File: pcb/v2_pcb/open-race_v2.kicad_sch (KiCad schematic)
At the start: 0 parts

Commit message: fnish micro sd card
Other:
- added sheet MicroSD (MicroSD.kicad_sch)
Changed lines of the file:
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@@
+	)
+	(sheet
+		(at 55.88 137.16)
+		(size 43.18 9.525)
+		(exclude_from_sim no)
+		(in_bom yes)
+		(on_board yes)
+		(dnp no)
+		(fields_autoplaced yes)
+		(stroke
+			(width 0.1524)
+			(type solid)
+		)
+		(fill
+			(color 0 0 0 0)
+		)
+		(property "Sheetname" "MicroSD"
+			(at 55.88 136.4484 0)
+			(show_name no)
+			(do_not_autoplace no)
+			(effects
+				(font
+					(size 1.27 1.27)
+				)
+				(justify left bottom)
+			)
+		)
+		(property "Sheetfile" "MicroSD.kicad_sch"
+			(at 55.88 147.2696 0)
+			(show_name no)
+			(do_not_autoplace no)
+			(effects
+				(font
+					(size 1.27 1.27)
+				)
+				(justify left top)
+			)
+		)
+		(instances
+			(project "open-race_v2"
+				(path "/1cc14db4-4207-4c76-b5f6-6a2491c5fa6b"
+					(page "9")
+				)
+			)
+		)
 	)
 	(sheet

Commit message: run load switch
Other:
- sheet Power ports: added PWR_ON; removed none
- sheet STM32_MCU_IO ports: added PWR_ON; removed none
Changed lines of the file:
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@@
 	(generator_version "10.0")
 	(paper "A4")
+	(wire
+		(pts
+			(xy 99.06 127) (xy 116.84 127)
+		)
+		(stroke
+			(width 0)
+			(type default)
+		)
+	)
 	(sheet
 		(at 55.88 83.82)
@@
 			)
 		)
+		(pin "PWR_ON" output
+			(at 116.84 127 180)
+			(effects
+				(font
+					(size 1.27 1.27)
+				)
+				(justify right)
+			)
+		)
 		(instances
 			(project "open-race_v2"
@@
 			)
 		)
+		(pin "PWR_ON" input
+			(at 99.06 127 0)
+			(effects
+				(font
+					(size 1.27 1.27)
+				)
+				(justify right)
+			)
+		)

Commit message: pcb done
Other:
- sheet Debug renamed SWD debug
- sheet HexaSPI_PSRAM renamed x16 PSRAM
- sheet MicroSD renamed microSD
- sheet OctoSPI_FLASH renamed Quad boot flash
- sheet STM32_MCU_IO renamed STM32 MCU I/O
- sheet STM32_MCU_PWR renamed STM32 power
- sheet USB renamed USB-C PD
- added sheet Buttons and LEDs (HMI.kicad_sch)
- added sheet ESP32-C6 radio (Radio_ESP32.kicad_sch)
- added sheet SCH16T IMU (IMU.kicad_sch)
- added sheet UM980 GNSS (GNSS.kicad_sch)
- sheet Power ports: added none; removed PWR_ON
- sheet STM32 MCU I/O ports: added none; removed PWR_ON
- sheet STM32 power ports: added none; removed MCUPower
- note added: "Cross-sheet connectivity uses scalar global labels. Display/backlight and buzzer are intentionally out of scope."
- note added: "GNSS / IMU"
- note added: "POWER / RADIO"
- note added: "STM32 / MEMORY"
- note added: "open-race v2 schematic"
- company: (none) -> open-race
- title: (none) -> open-race v2

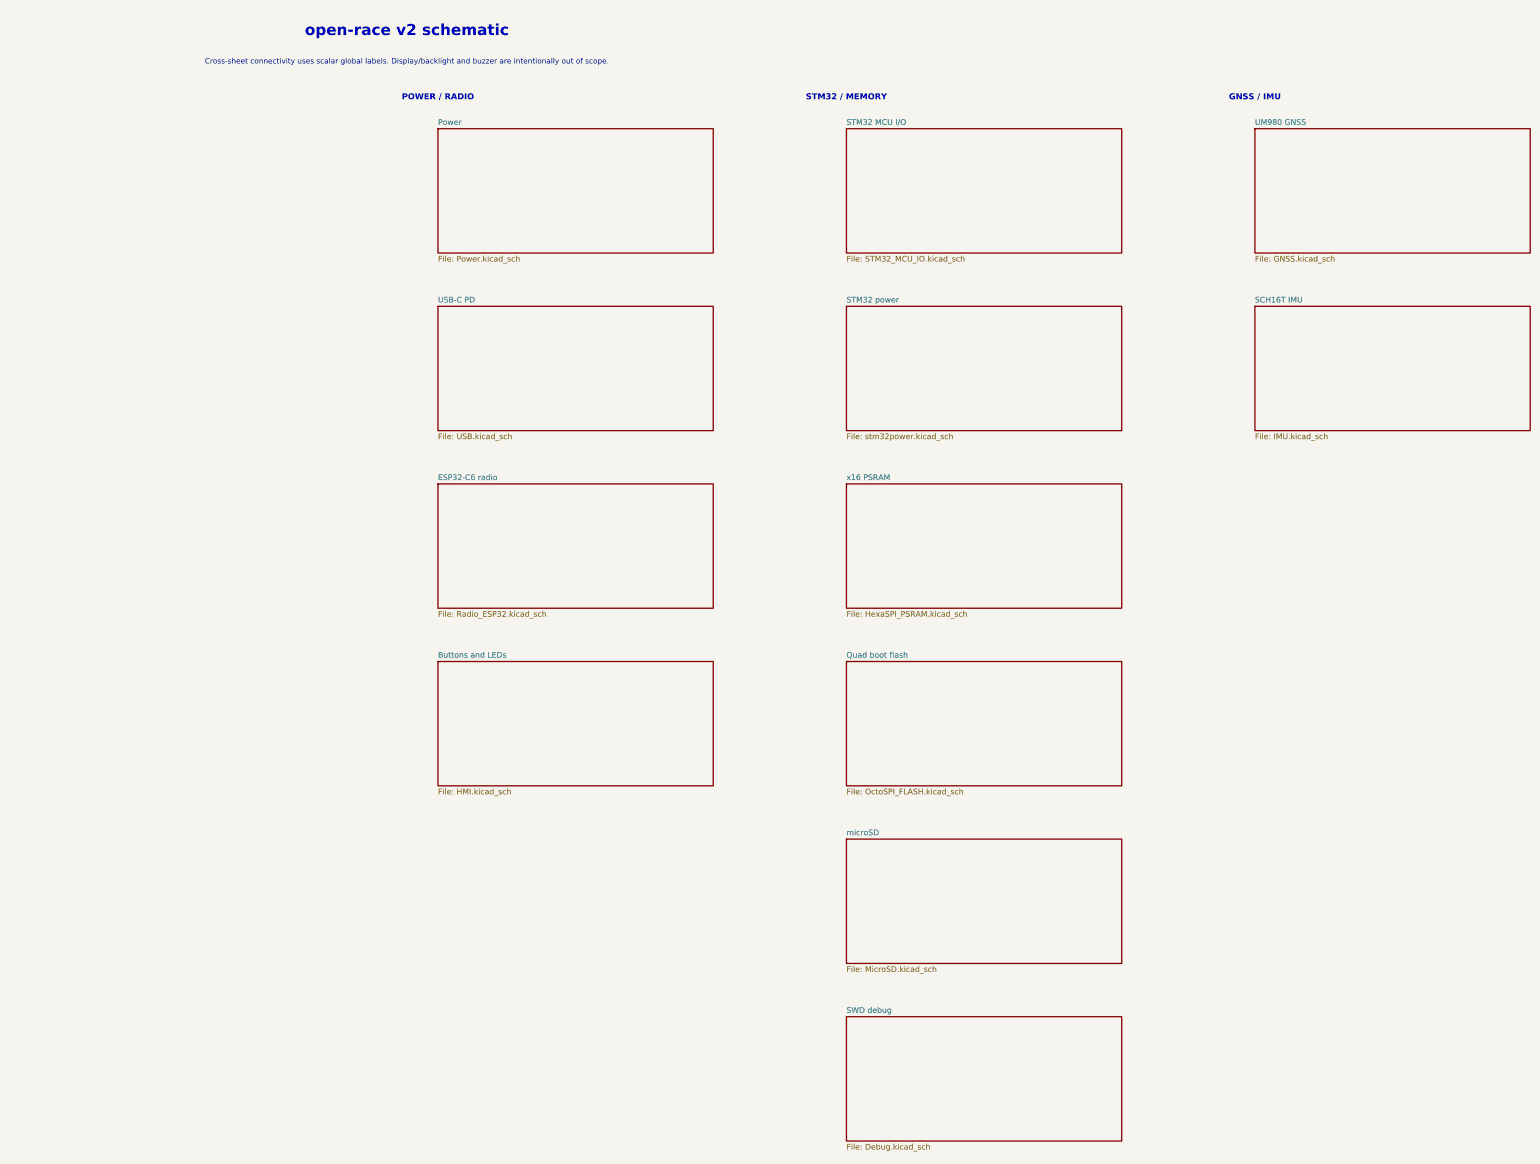
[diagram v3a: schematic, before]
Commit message: switch mosfets
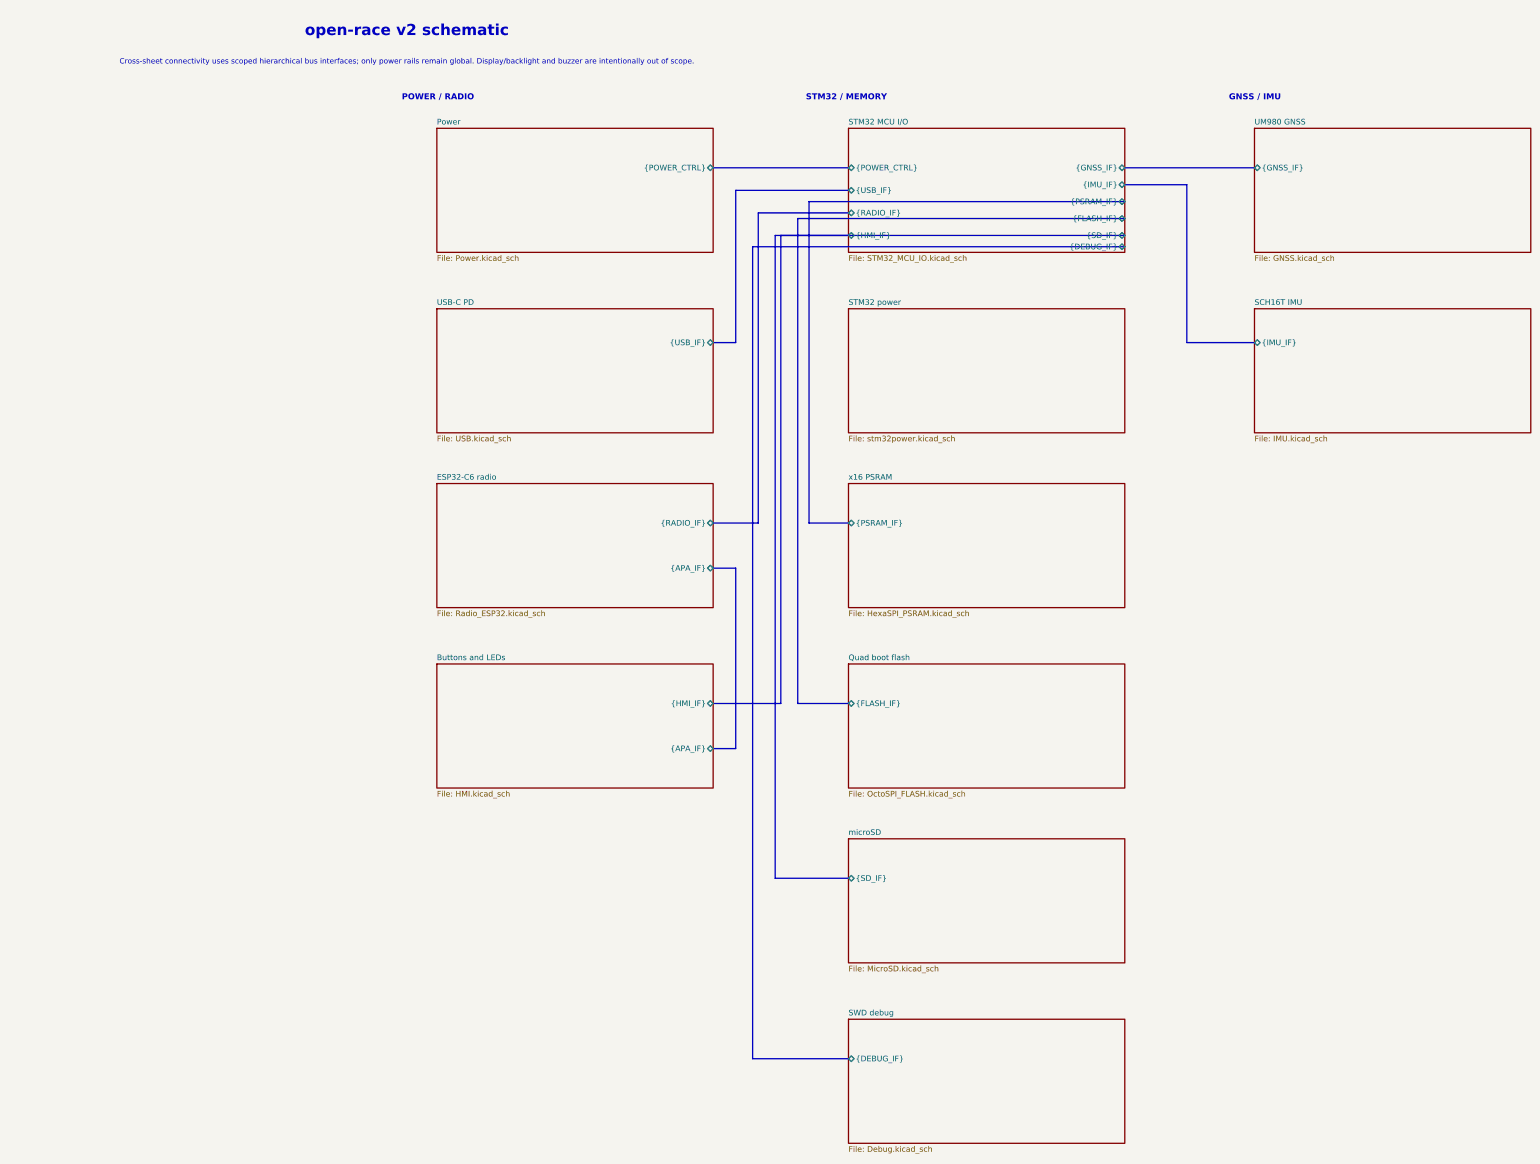
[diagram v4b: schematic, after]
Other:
- sheet Buttons and LEDs ports: added {APA_IF}, {HMI_IF}; removed none
- sheet ESP32-C6 radio ports: added {APA_IF}, {RADIO_IF}; removed none
- sheet Power ports: added {POWER_CTRL}; removed none
- sheet Quad boot flash ports: added {FLASH_IF}; removed none
- sheet SCH16T IMU ports: added {IMU_IF}; removed none
- sheet STM32 MCU I/O ports: added {DEBUG_IF}, {FLASH_IF}, {GNSS_IF}, {HMI_IF}, {IMU_IF}, {POWER_CTRL}, {PSRAM_IF}, {RADIO_IF}, {SD_IF}, {USB_IF}; removed none
- sheet SWD debug ports: added {DEBUG_IF}; removed none
- sheet UM980 GNSS ports: added {GNSS_IF}; removed none
- sheet USB-C PD ports: added {USB_IF}; removed none
- sheet microSD ports: added {SD_IF}; removed none
- sheet x16 PSRAM ports: added {PSRAM_IF}; removed none
- note added: "Cross-sheet connectivity uses scoped hierarchical bus interfaces; only power rails remain global. Display/backlight and buzzer are intentionally out of scope."
- note removed: "Cross-sheet connectivity uses scalar global labels. Display/backlight and buzzer are intentionally out of scope."
